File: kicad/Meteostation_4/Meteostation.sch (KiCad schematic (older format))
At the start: 110 parts, among them J1 TxD, J10 GM+, J11 GM-, J12 SWD, J13 SWC, J14 DISP_CS, J2 RxD, J3 BME280_SCL, J4 BME280_SDA, J5 miso, J6 +EXT, J7 -EXT, J8 mosi, J9 sclk, Q1 5N10, Q2 IRLML6346, Q3 Q_NPN_BEC, T1 HY931147C, U1 STM32F103C8Tx, U2 LMR14206, U3 AD8541, Y2 ECS-250-20-33 25MHz

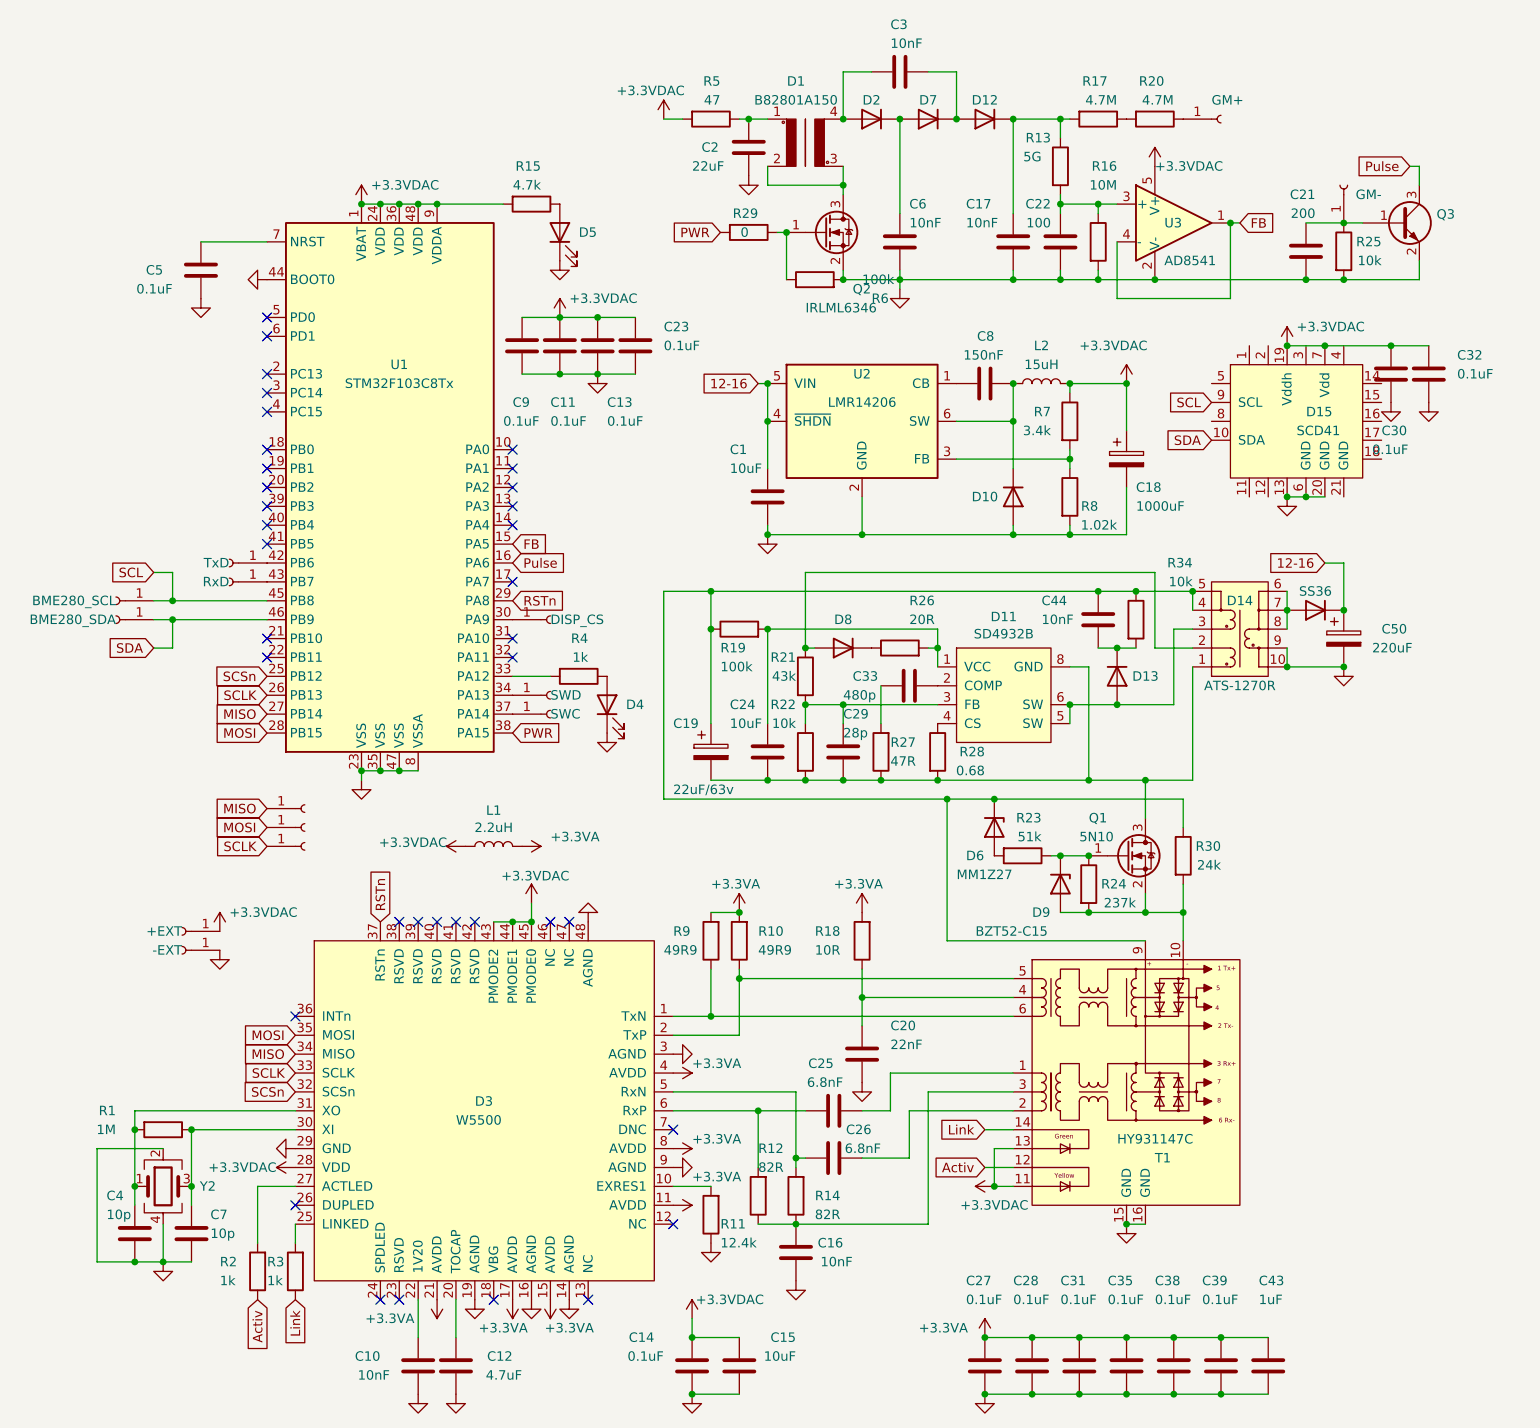
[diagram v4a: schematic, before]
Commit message: изменено:      Documents/sheet.png 	изменено:      kicad/Meteostation_4/Meteostation-cache.lib 	изменено:      kicad/Meteostation_4/Meteostation.kicad_pcb 	изменено:      kicad/Meteostation_4/Meteostation.kicad_pcb-bak 	изменено:      kicad/Meteostation_4/Meteostation.sch 	изменено:      kicad/Meteostation_4/Meteostation.sch-bak 	изменено:      kicad/Meteostation_4/fp-info-cache 	изменено:      stm32cubeide/Meteostation/.mxproject 	изменено:      stm32cubeide/Meteostation/.settings/language.settings.xml 	изменено:      stm32cubeide/Meteostation/Core/Inc/main.h 	изменено:      stm32cubeide/Meteostation/Core/Src/main.c 	изменено:      stm32cubeide/Meteostation/Meteostation.ioc 	изменено:      stm32cubeide/Meteostation/Release/Core/Src/main.o 	изменено:      stm32cubeide/Meteostation/Release/Core/Src/main.su 	изменено:      stm32cubeide/Meteostation/Release/Meteostation.bin 	изменено:      stm32cubeide/Meteostation/Release/Meteostation.elf 	изменено:      stm32cubeide/Meteostation/Release/Meteostation.hex 	изменено:      stm32cubeide/Meteostation/Release/Meteostation.list 	изменено:      stm32cubeide/Meteostation/Release/Meteostation.map 	изменено:      stm32cubeide/Meteostation/Release/makefile
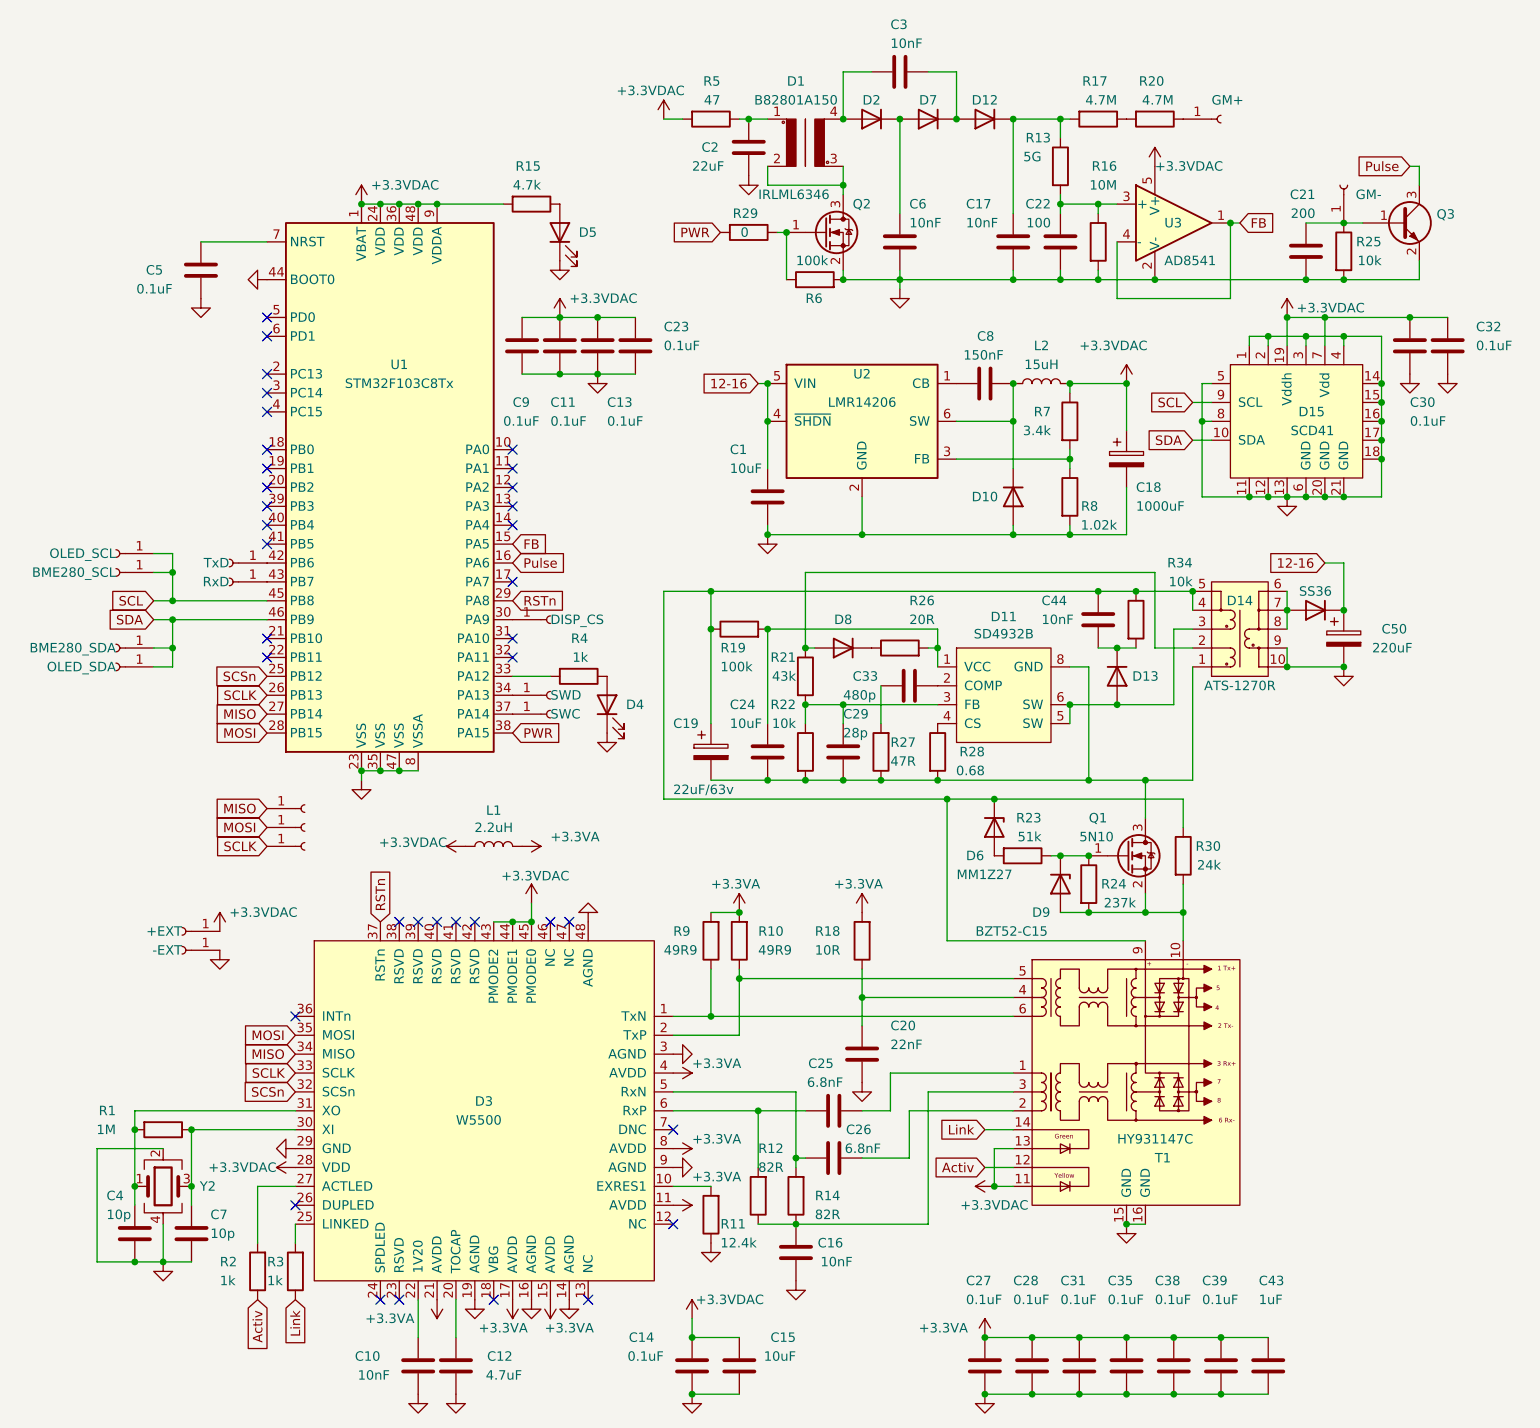
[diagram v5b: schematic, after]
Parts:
- removed D15: SCD41, My-library:SCD41, symbol Meteostation-rescue:SCD41-My_Library
- added D15: SCD41, My-library:SCD41, symbol My_Library:SCD41
- added J15: OLED_SCL, My-library:SMD-CONN, symbol Connector:Conn_01x01_Female
- added J16: OLED_SDA, My-library:SMD-CONN, symbol Connector:Conn_01x01_Female
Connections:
- net +3.3VDAC: now also D15.19 (Vddh), D15.7 (Vdd)
- net GND: now also D15.1, D15.11, D15.12, D15.13, D15.14, D15.15, D15.16, D15.17, D15.18, D15.2, D15.20 (GND), D15.21 (GND), D15.3, D15.4, D15.5, D15.6 (GND), D15.8
- net SCL: now also D15.9 (SCL), J15.1 (Pin_1)
- net SDA: now also D15.10 (SDA), J16.1 (Pin_1)
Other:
- moved on the sheet: C30, C32
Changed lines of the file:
@@
 L Connector:Conn_01x01_Female J3
 U 1 1 625660A2
-P 4050 5250
-F 0 "J3" H 3550 5250 50  0001 C CNN
-F 1 "BME280_SCL" H 4050 5250 50  0000 L CNN
-F 2 "My-library:SMD-CONN" H 4050 5250 50  0001 C CNN
-F 3 "~" H 4050 5250 50  0001 C CNN
-	1    4050 5250
+P 4050 5100
+F 0 "J3" H 3550 5100 50  0001 C CNN
+F 1 "BME280_SCL" H 4050 5100 50  0000 L CNN
+F 2 "My-library:SMD-CONN" H 4050 5100 50  0001 C CNN
+F 3 "~" H 4050 5100 50  0001 C CNN
+	1    4050 5100
 	-1   0    0    1
 $EndComp
@@
 L Connector:Conn_01x01_Female J4
 U 1 1 62569E06
-P 4050 5350
-F 0 "J4" H 3550 5350 50  0001 C CNN
-F 1 "BME280_SDA" H 4050 5350 50  0000 L CNN
-F 2 "My-library:SMD-CONN" H 4050 5350 50  0001 C CNN
-F 3 "~" H 4050 5350 50  0001 C CNN
-	1    4050 5350
+P 4050 5500
+F 0 "J4" H 3550 5500 50  0001 C CNN
+F 1 "BME280_SDA" H 4050 5500 50  0000 L CNN
+F 2 "My-library:SMD-CONN" H 4050 5500 50  0001 C CNN
+F 3 "~" H 4050 5500 50  0001 C CNN
+	1    4050 5500
 	-1   0    0    1
 $EndComp
@@
 NoConn ~ 4850 4850
 $Comp
-L Meteostation-rescue:SCD41-My_Library D15
-U 1 1 640A44F0
-P 10250 4300
-F 0 "D15" H 10350 4350 50  0000 L CNN
-F 1 "SCD41" H 10300 4250 50  0000 L CNN
-F 2 "My-library:SCD41" H 10250 4300 50  0001 C CNN
-F 3 "" H 10250 4300 50  0001 C CNN
-	1    10250 4300
-	1    0    0    -1
-$EndComp
-$Comp
 L power:GND #PWR0101
 U 1 1 640CEE82
@@
 	1    0    0    -1
 $EndComp
-Wire Wire Line
-	10250 4700 10350 4700
-Connection ~ 10250 4700
-Connection ~ 10350 4700
-Wire Wire Line
-	10350 4700 10450 4700
 $Comp
 L power:+3.3VDAC #PWR0102
 U 1 1 640DDD17
-P 10250 3900
-F 0 "#PWR0102" H 10400 3850 50  0001 C CNN
-F 1 "+3.3VDAC" H 10300 4000 50  0000 L CNN
-F 2 "" H 10250 3900 50  0001 C CNN
-F 3 "" H 10250 3900 50  0001 C CNN
-	1    10250 3900
-	1    0    0    -1
-$EndComp
-Wire Wire Line
-	10250 3900 10450 3900
-Connection ~ 10250 3900
-Text GLabel 9850 4200 0    50   Input ~ 0
+P 10250 3750
+F 0 "#PWR0102" H 10400 3700 50  0001 C CNN
+F 1 "+3.3VDAC" H 10300 3800 50  0000 L CNN
+F 2 "" H 10250 3750 50  0001 C CNN
+F 3 "" H 10250 3750 50  0001 C CNN
+	1    10250 3750
+	1    0    0    -1
+$EndComp
+Text GLabel 9750 4200 0    50   Input ~ 0
 SCL
-Text GLabel 9850 4400 0    50   Input ~ 0
+Text GLabel 9750 4400 0    50   Input ~ 0
 SDA
-Text GLabel 4250 5100 0    50   Input ~ 0
+Text GLabel 4250 5250 0    50   Input ~ 0
 SCL
-Text GLabel 4250 5500 0    50   Input ~ 0
+Text GLabel 4250 5350 0    50   Input ~ 0
 SDA
 Wire Wire Line
@@
 L Device:C C30
 U 1 1 631FC205
-P 10800 4050
-F 0 "C30" H 10750 3750 50  0000 L CNN
-F 1 "0.1uF" H 10700 3650 50  0000 L CNN
-F 2 "Capacitor_SMD:C_0603_1608Metric" H 10838 3900 50  0001 C CNN
-F 3 "~" H 10800 4050 50  0001 C CNN
-	1    10800 4050
+P 10900 3900
+F 0 "C30" H 10900 3600 50  0000 L CNN
+F 1 "0.1uF" H 10900 3500 50  0000 L CNN
+F 2 "Capacitor_SMD:C_0603_1608Metric" H 10938 3750 50  0001 C CNN
+F 3 "~" H 10900 3900 50  0001 C CNN
+	1    10900 3900
 	1    0    0    -1
 $EndComp
@@
 L Device:C C32
 U 1 1 631FD7A8
-P 11000 4050
-F 0 "C32" H 11150 4150 50  0000 L CNN
-F 1 "0.1uF" H 11150 4050 50  0000 L CNN
-F 2 "Capacitor_SMD:C_0603_1608Metric" H 11038 3900 50  0001 C CNN
-F 3 "~" H 11000 4050 50  0001 C CNN
-	1    11000 4050
-	1    0    0    -1
-$EndComp
-Wire Wire Line
-	10450 3900 10800 3900
-Connection ~ 10450 3900
+P 11100 3900
+F 0 "C32" H 11250 4000 50  0000 L CNN
+F 1 "0.1uF" H 11250 3900 50  0000 L CNN
+F 2 "Capacitor_SMD:C_0603_1608Metric" H 11138 3750 50  0001 C CNN
+F 3 "~" H 11100 3900 50  0001 C CNN
+	1    11100 3900
+	1    0    0    -1
+$EndComp
 $Comp
 L power:GND #PWR041
 U 1 1 6320F99D
-P 10800 4200
-F 0 "#PWR041" H 10800 3950 50  0001 C CNN
-F 1 "GND" H 10805 4027 50  0001 C CNN
-F 2 "" H 10800 4200 50  0001 C CNN
-F 3 "" H 10800 4200 50  0001 C CNN
-	1    10800 4200
+P 10900 4050
+F 0 "#PWR041" H 10900 3800 50  0001 C CNN
+F 1 "GND" H 10905 3877 50  0001 C CNN
+F 2 "" H 10900 4050 50  0001 C CNN
+F 3 "" H 10900 4050 50  0001 C CNN
+	1    10900 4050
 	1    0    0    -1
 $EndComp
@@
 L power:GND #PWR042
 U 1 1 63210EED
-P 11000 4200
-F 0 "#PWR042" H 11000 3950 50  0001 C CNN
-F 1 "GND" H 11005 4027 50  0001 C CNN
-F 2 "" H 11000 4200 50  0001 C CNN
-F 3 "" H 11000 4200 50  0001 C CNN
-	1    11000 4200
+P 11100 4050
+F 0 "#PWR042" H 11100 3800 50  0001 C CNN
+F 1 "GND" H 11105 3877 50  0001 C CNN
+F 2 "" H 11100 4050 50  0001 C CNN
+F 3 "" H 11100 4050 50  0001 C CNN
+	1    11100 4050
 	1    0    0    -1
 $EndComp
@@
 	1    0    0    -1
 $EndComp
-Connection ~ 10800 3900
-Wire Wire Line
-	10800 3900 11000 3900
+Wire Wire Line
+	10900 3750 11100 3750
 Wire Wire Line
 	7550 3300 7600 3300
@@
 U 1 1 634FB19F
 P 7750 3550
-F 0 "R6" V 7650 3250 50  0000 R CNN
-F 1 "100k" V 7750 3300 50  0000 R CNN
+F 0 "R6" V 7650 3600 50  0000 R CNN
+F 1 "100k" V 7850 3650 50  0000 R CNN
 F 2 "Resistor_SMD:R_0603_1608Metric" V 7680 3550 50  0001 C CNN
 F 3 "~" H 7750 3550 50  0001 C CNN
@@
 U 1 1 6364CAE8
 P 7800 3300
-F 0 "Q2" H 7950 3000 50  0000 L CNN
-F 1 "IRLML6346" H 7700 2900 50  0000 L CNN
+F 0 "Q2" H 7950 3450 50  0000 L CNN
+F 1 "IRLML6346" H 7450 3500 50  0000 L CNN
 F 2 "Package_TO_SOT_SMD:SOT-23" H 8000 3225 50  0001 L CIN
 F 3 "https://www.onsemi.com/pub/Collateral/BSS138-D.PDF" H 7800 3300 50  0001 L CNN
@@
 	7450 4100 7500 4100
 Connection ~ 7500 4100
+$Comp
+L My_Library:SCD41 D15
+U 1 1 63BEA614
+P 10250 4300
+F 0 "D15" H 10450 4350 50  0000 R CNN
+F 1 "SCD41" H 10500 4250 50  0000 R CNN
+F 2 "My-library:SCD41" H 10250 4300 50  0001 C CNN
+F 3 "" H 10250 4300 50  0001 C CNN
+	1    10250 4300
+	1    0    0    -1
+$EndComp
+Wire Wire Line
+	10350 4700 10450 4700
+Wire Wire Line
+	10050 3900 10050 3850
+Wire Wire Line
+	10750 4700 10550 4700
+Connection ~ 10750 4100
+Wire Wire Line
+	10750 4100 10750 4200
+Connection ~ 10750 4200
+Wire Wire Line
+	10750 4200 10750 4300
+Connection ~ 10750 4300
+Wire Wire Line
+	10750 4300 10750 4400
+Connection ~ 10750 4400
+Wire Wire Line
+	10750 4400 10750 4500
+Connection ~ 10750 4500
+Wire Wire Line
+	10750 4500 10750 4700
+Connection ~ 10450 4700
+Connection ~ 10550 4700
+Wire Wire Line
+	10550 4700 10450 4700
+Wire Wire Line
+	10050 4700 10150 4700
+Connection ~ 10350 4700
+Connection ~ 10150 4700
+Wire Wire Line
+	10150 4700 10250 4700
+Connection ~ 10250 4700
+Wire Wire Line
+	10250 4700 10350 4700
+Wire Wire Line
+	9750 4200 9850 4200
+Wire Wire Line
+	9750 4400 9850 4400
+Wire Wire Line
+	9850 4100 9800 4100
+Wire Wire Line
+	9800 4100 9800 4300
+Wire Wire Line
+	9800 4700 10050 4700
+Connection ~ 10050 4700
+Wire Wire Line
+	9850 4300 9800 4300
+Connection ~ 9800 4300
+Wire Wire Line
+	9800 4300 9800 4700
+Wire Wire Line
+	10050 3850 10150 3850
+Wire Wire Line
+	10750 3850 10750 4100
+Wire Wire Line
+	10150 3900 10150 3850
+Connection ~ 10150 3850
+Wire Wire Line
+	10150 3850 10350 3850
+Wire Wire Line
+	10350 3900 10350 3850
+Connection ~ 10350 3850
+Wire Wire Line
+	10350 3850 10550 3850
+Wire Wire Line
+	10550 3900 10550 3850
+Connection ~ 10550 3850
+Wire Wire Line
+	10550 3850 10750 3850
+Wire Wire Line
+	10450 3750 10450 3900
+Wire Wire Line
+	10250 3900 10250 3750
+Wire Wire Line
+	10250 3750 10450 3750
+Connection ~ 10250 3750
+Wire Wire Line
+	10450 3750 10900 3750
+Connection ~ 10450 3750
+Connection ~ 10900 3750
+$Comp
+L Connector:Conn_01x01_Female J15
+U 1 1 63E515E7
+P 4050 5000
+F 0 "J15" H 3550 5000 50  0001 C CNN
+F 1 "OLED_SCL" H 4050 5000 50  0000 L CNN
+F 2 "My-library:SMD-CONN" H 4050 5000 50  0001 C CNN
+F 3 "~" H 4050 5000 50  0001 C CNN
+	1    4050 5000
+	-1   0    0    1
+$EndComp
+$Comp
+L Connector:Conn_01x01_Female J16
+U 1 1 63E51E30
+P 4050 5600
+F 0 "J16" H 3550 5600 50  0001 C CNN
+F 1 "OLED_SDA" H 4050 5600 50  0000 L CNN
+F 2 "My-library:SMD-CONN" H 4050 5600 50  0001 C CNN
+F 3 "~" H 4050 5600 50  0001 C CNN
+	1    4050 5600
+	-1   0    0    1
+$EndComp
+Wire Wire Line
+	4250 5000 4350 5000
+Wire Wire Line
+	4350 5000 4350 5100
+Connection ~ 4350 5100
+Wire Wire Line
+	4350 5500 4350 5600
+Wire Wire Line
+	4350 5600 4250 5600
+Connection ~ 4350 5500
 $EndSCHEMATC
